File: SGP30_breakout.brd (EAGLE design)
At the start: 11.6 x 17.5 mm, 12 parts, among them IC1 MCP1703T-1802E/CB, Q1 220mA/50V/3.5Ω, Q2 220mA/50V/3.5Ω

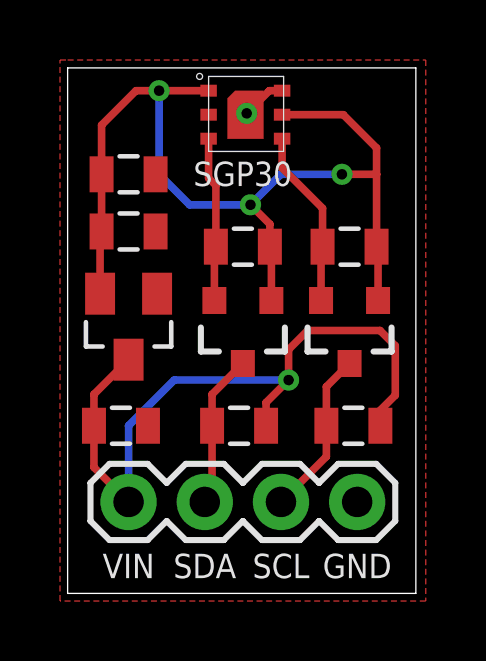
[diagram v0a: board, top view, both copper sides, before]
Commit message: R2 - bug fixes
- GND and SCL trace swapped
- shrinked board size
- silkscreen adjustments
- removed GND plane
- routed GND trace
- trace adjustments
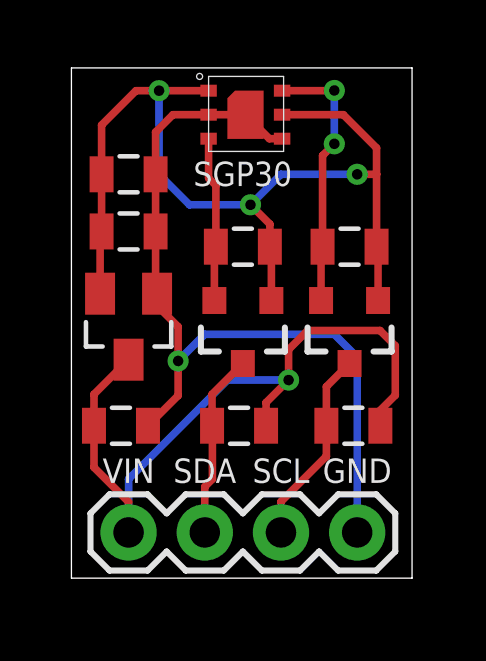
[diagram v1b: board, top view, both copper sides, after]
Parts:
- moved J1 1.02 mm to (9.65, 3.05)
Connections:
- net GND: now also U$1.P$6; no longer U$1.P$4
- net SCL_1V8: now also U$1.P$4; no longer U$1.P$6
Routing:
- net GND: track 1.62 -> 27.8 mm
- net SCL_1V8: track 5.97 -> 8.93 mm, vias 0 -> 2
- net SCL: track 5.56 -> 6.59 mm
- net SDA: track 5.14 -> 6.17 mm
- net VIN: track 24.0 -> 24.9 mm
- removed copper zone on layer 1, net GND
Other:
- board size 11.6 x 17.5 mm -> 11.4 x 17 mm
- board text added: "R2 - 2017"
- board text removed: "R1 - 2017"
